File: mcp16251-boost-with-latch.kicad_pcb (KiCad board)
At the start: 2 copper layers, 33 x 22.9 mm, 30 parts, among them J1 THT_Castellated, J10 THT_Castellated, J11 SMD_pad, J2 THT_Castellated, J3 THT_Castellated, J4 SMD_pad, J5 SMD_pad, J6 SMD_pad, J7 SMD_pad, J8 SMD_pad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

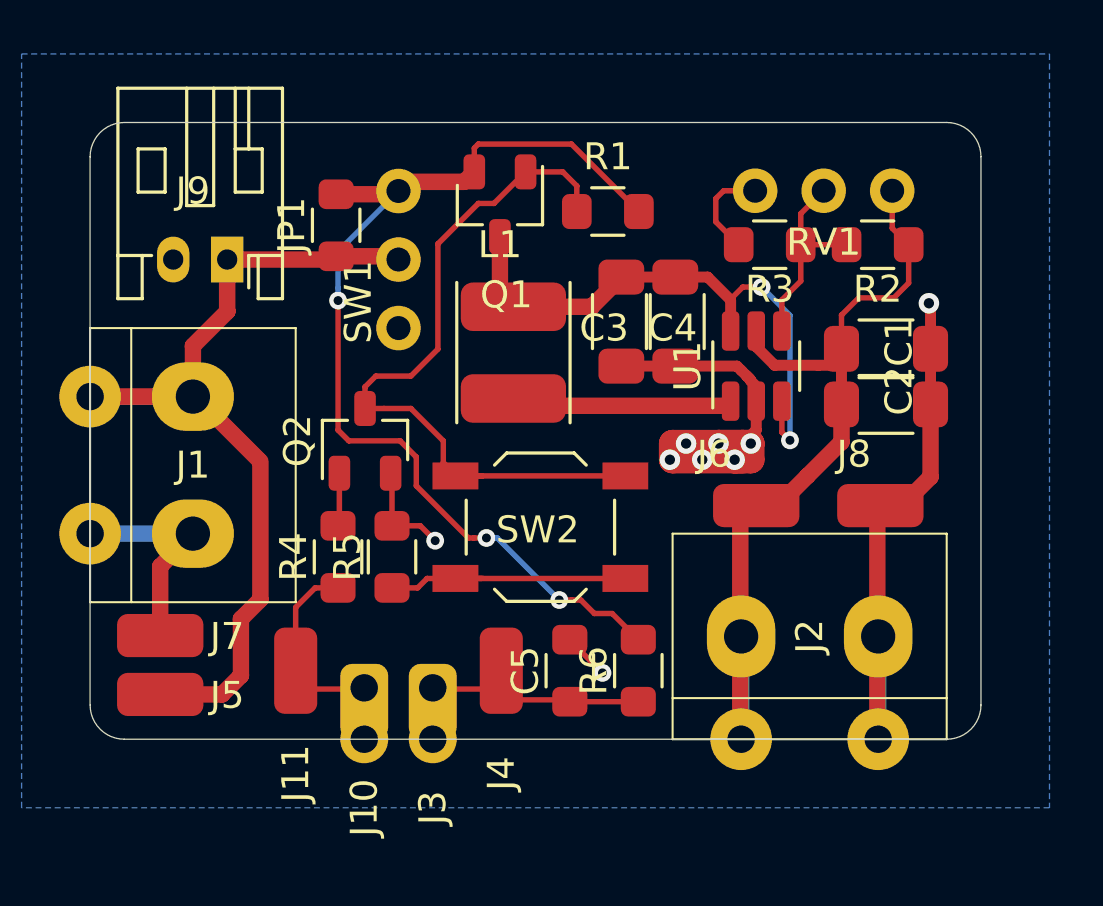
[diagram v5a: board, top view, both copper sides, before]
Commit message: Silkscreen texts
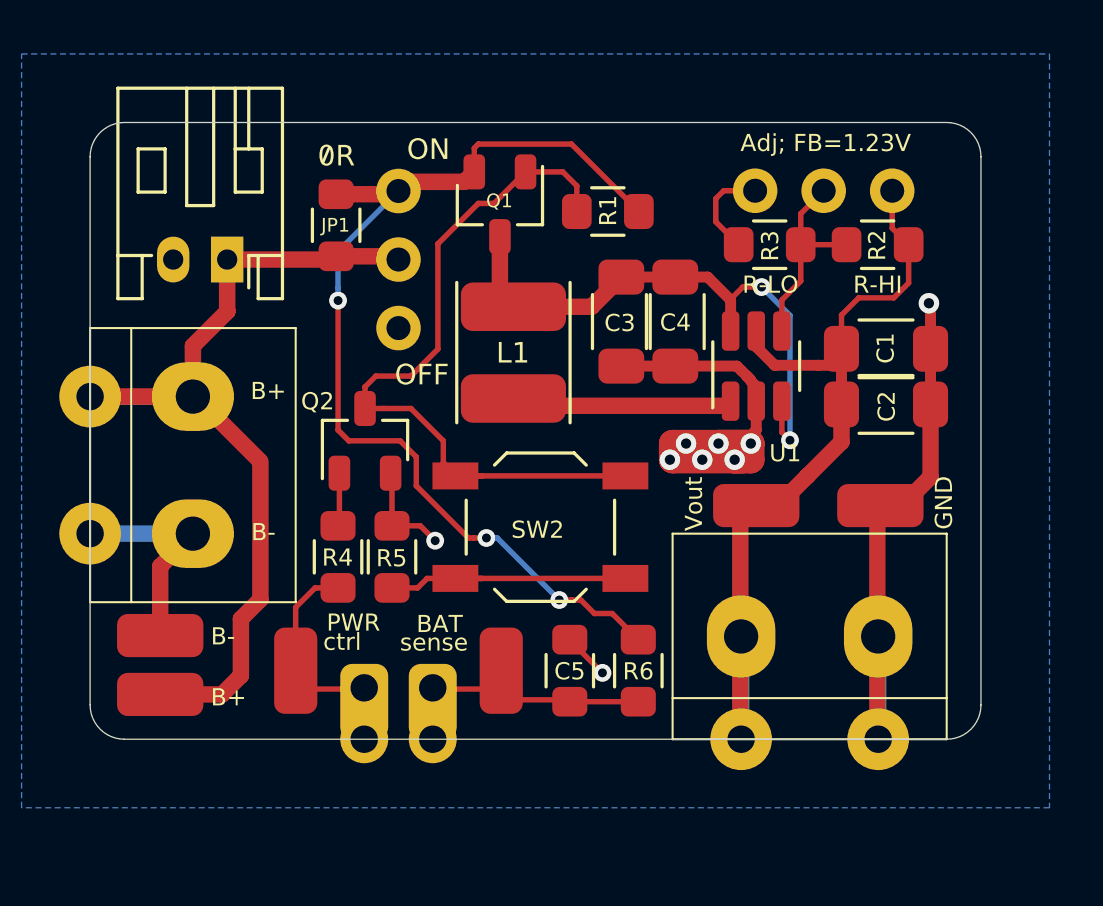
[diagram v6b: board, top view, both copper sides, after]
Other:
- board text added: "0R"
- board text added: "Adj; FB=1.23V"
- board text added: "B+"
- board text added: "B-"
- board text added: "B- GND"
- board text added: "BAT"
- board text added: "BAT sense"
- board text added: "FB"
- board text added: "GND"
- board text added: "GND B-"
- board text added: "MCP16251T boost module rev. 1 (c) Vlad Belous; CC BY-SA"
- board text added: "OFF"
- board text added: "ON"
- board text added: "PWR"
- board text added: "PWR control"
- board text added: "R-HI"
- board text added: "R-LO"
- board text added: "VOUT"
- board text added: "Vout"
- board text added: "ctrl"
- board text added: "sense"

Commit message: Adjustments
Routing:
- net GND: track 53.0 -> 57.2 mm, vias 9 -> 12
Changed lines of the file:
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@@
     (thickness 1.6)
     (drawings 41)
-    (tracks 176)
+    (tracks 186)
     (zones 0)
     (modules 30)
@@
   )
   (setup
-    (last_trace_width 0.2032)
+    (last_trace_width 0.4064)
     (user_trace_width 0.2032)
     (user_trace_width 0.4064)
@@
     (tags SOT-23-6)
     (attr smd)
-    (fp_text reference U1 (at -3.23312 1.07576 180) (layer F.SilkS)
+    (fp_text reference U1 (at -1.7396 -2.4396 180) (layer F.SilkS)
       (effects (font (size 0.635 0.635) (thickness 0.1016)))
     )
@@
   (segment (start 161.29 90.01) (end 161.29 90.79) (width 0.6096) (layer F.Cu) (net 2))
   (segment (start 161.96 89.34) (end 161.29 90.01) (width 0.6096) (layer F.Cu) (net 2))
-  (segment (start 161.96 86.65) (end 161.96 89.34) (width 0.6096) (layer F.Cu) (net 2))
   (segment (start 134.62 91.44) (end 131.33071 91.44) (width 0.6096) (layer B.Cu) (net 2))
   (segment (start 160.02 95.25) (end 160.02 98.53929) (width 0.6096) (layer B.Cu) (net 2))
@@
   (segment (start 161.96 82.96) (end 161.9 82.9) (width 0.4064) (layer F.Cu) (net 2))
   (segment (start 161.96 84.59) (end 161.96 82.96) (width 0.4064) (layer F.Cu) (net 2))
+  (segment (start 160.1 88.6752) (end 160.0962 88.6714) (width 0.4064) (layer F.Cu) (net 2))
+  (via (at 160.0962 88.6714) (size 0.762) (drill 0.381) (layers F.Cu B.Cu) (net 2))
+  (segment (start 160.1 90.4) (end 160.1 88.6752) (width 0.4064) (layer F.Cu) (net 2))
+  (segment (start 162.7378 88.3412) (end 162.7632 88.3666) (width 0.4064) (layer F.Cu) (net 2))
+  (segment (start 161.96 88.3412) (end 162.7378 88.3412) (width 0.4064) (layer F.Cu) (net 2))
+  (via (at 162.7632 88.3666) (size 0.762) (drill 0.381) (layers F.Cu B.Cu) (net 2))
+  (segment (start 161.96 86.65) (end 161.96 88.3412) (width 0.6096) (layer F.Cu) (net 2))
+  (segment (start 161.96 88.3412) (end 161.96 89.34) (width 0.6096) (layer F.Cu) (net 2))
+  (via (at 160.3756 86.6394) (size 0.762) (drill 0.381) (layers F.Cu B.Cu) (net 2))
+  (segment (start 160.3862 86.65) (end 160.3756 86.6394) (width 0.4064) (layer F.Cu) (net 2))
+  (segment (start 161.96 86.65) (end 160.3862 86.65) (width 0.4064) (layer F.Cu) (net 2))
   (via (at 156.75 87.98) (size 0.6604) (drill 0.3302) (layers F.Cu B.Cu) (net 3))
   (segment (start 156.45 87.68) (end 156.75 87.98) (width 0.2032) (layer F.Cu) (net 3))
